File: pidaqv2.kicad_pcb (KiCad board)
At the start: 2 copper layers, 81.3 x 88.9 mm, 28 parts, among them J101 Screw_Terminal_01x11, J102 Screw_Terminal_01x06, J103 Conn_01x02_Male, J104 Screw_Terminal_01x04, J105 Screw_Terminal_01x08, U201 ADS1261BIRHBR, U301 ADS1261BIRHBR, U401 AD8426ACPZ-R7

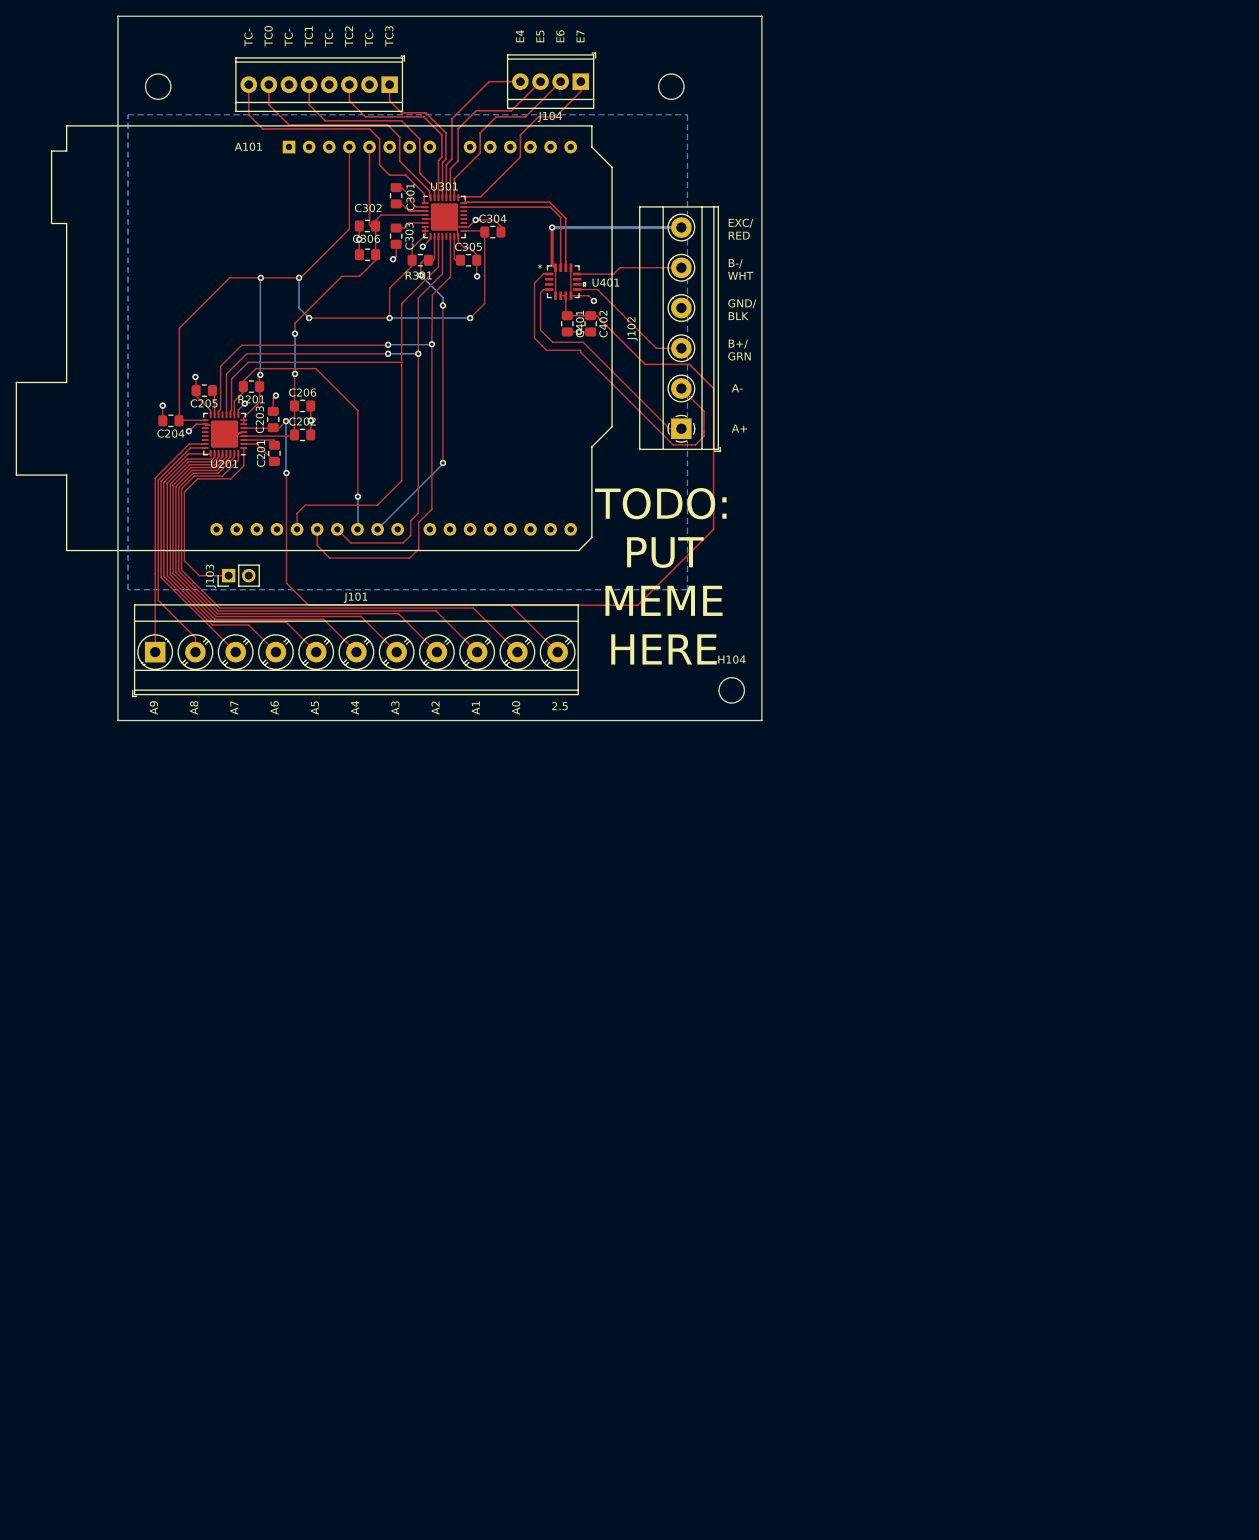
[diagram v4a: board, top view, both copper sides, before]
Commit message: placed general sensors chip
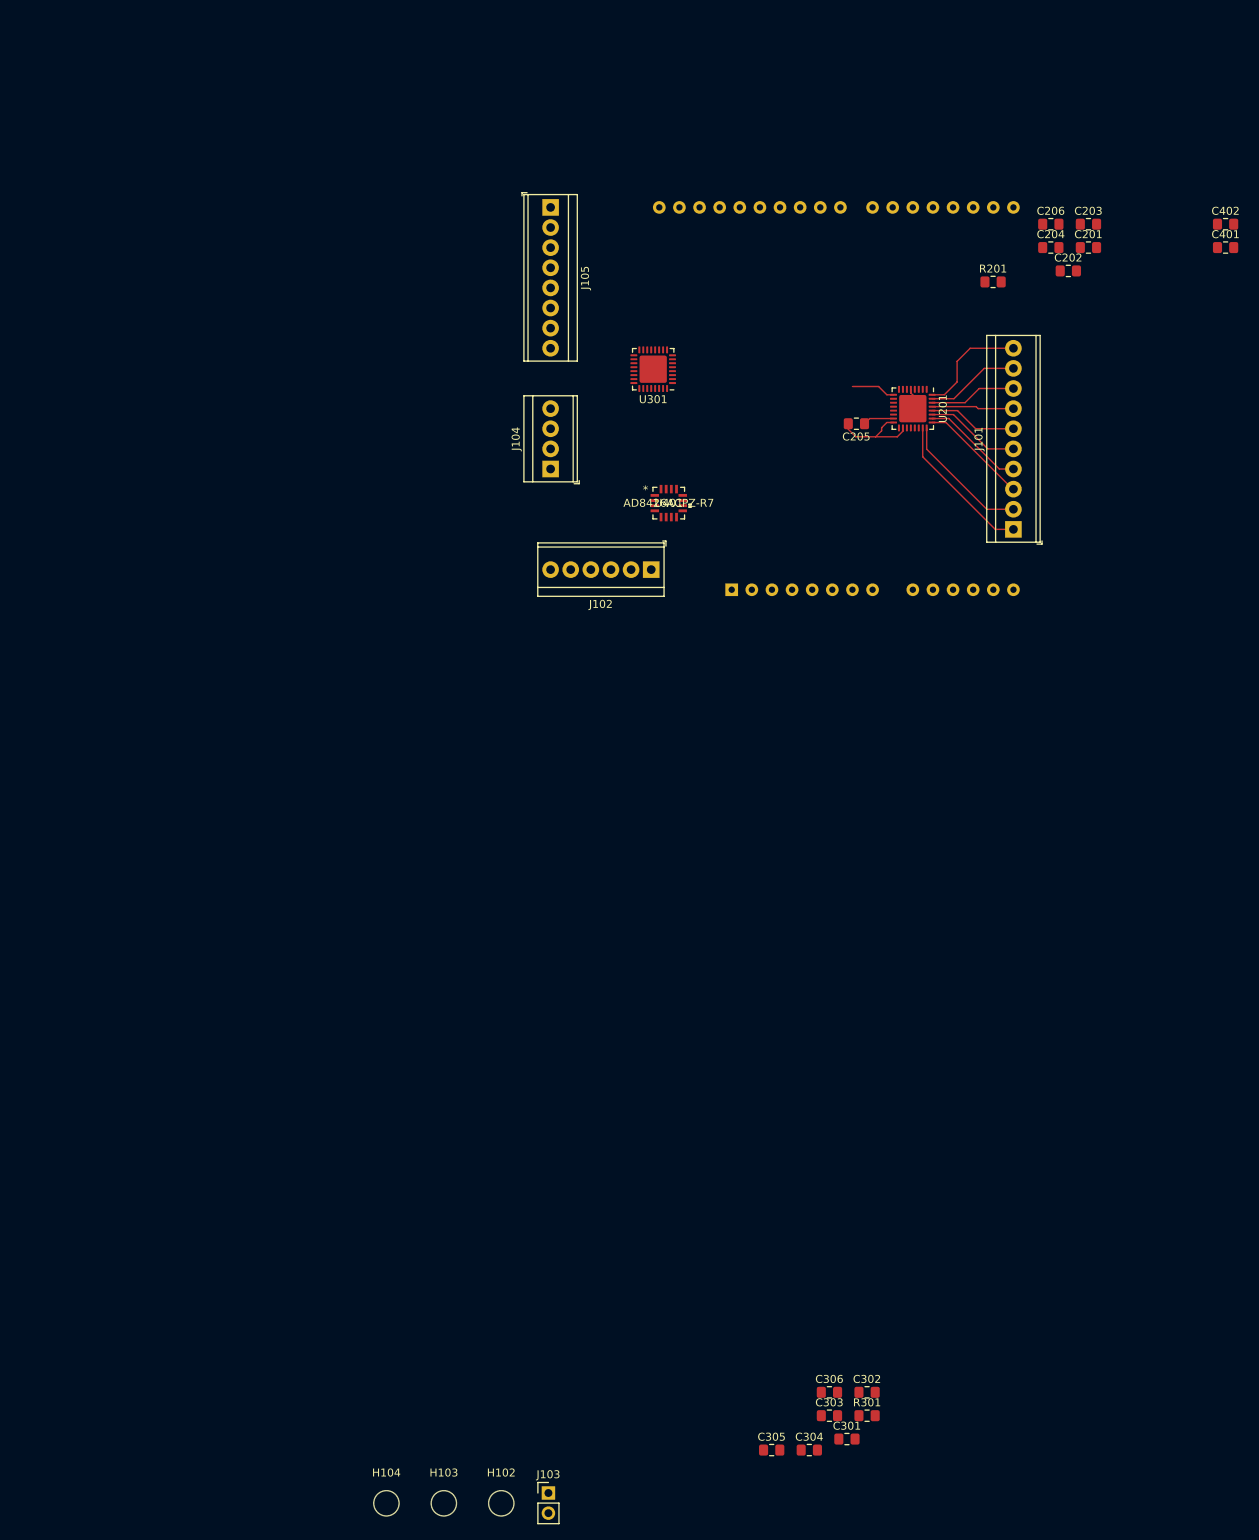
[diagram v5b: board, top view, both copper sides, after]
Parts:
- A101: moved to B.Cu
- J101: value Screw_Terminal_01x11 -> Screw_Terminal_01x10; footprint TerminalBlock_Phoenix:TerminalBlock_Phoenix_MKDS-3-11-5.08_1x11_P5.08mm_Horizontal -> TerminalBlock_TE-Connectivity:TerminalBlock_TE_1-282834-0_1x10_P2.54mm_Horizontal
- J102: footprint TerminalBlock_Phoenix:TerminalBlock_Phoenix_MKDS-1,5-6-5.08_1x06_P5.08mm_Horizontal -> TerminalBlock_TE-Connectivity:TerminalBlock_TE_282834-6_1x06_P2.54mm_Horizontal
- moved H103 182.4 mm to (105.9, 242.3)
- moved H102 180.1 mm to (113.2, 242.3)
- moved C301 166.9 mm to (156.8, 234.2), turned to 0 degrees
- moved C302 160.2 mm to (159.3, 228.3), turned to 0 degrees
- moved C304 158.8 mm to (152.0, 235.6)
- moved C303 158.6 mm to (154.6, 231.3), turned to 0 degrees
- moved R301 156.4 mm to (159.3, 231.3)
- moved C305 155.0 mm to (147.3, 235.6)
- moved C306 155.0 mm to (154.6, 228.3), turned to 0 degrees
- moved J103 122.6 mm to (119.1, 241.0), turned to 0 degrees
- moved C204 113.2 mm to (182.5, 83.8), turned to 0 degrees
- moved H104 111.5 mm to (98.7, 242.3)
- moved J101 109.4 mm to (177.8, 119.4), turned to 90 degrees
- moved C201 106.0 mm to (187.3, 83.8), turned to 0 degrees
- moved C203 105.8 mm to (187.3, 80.9), turned to 0 degrees
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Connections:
- C202 pad 2: GND -> GNDREF
- C203 pad 1: 2.5V -> /ADC0/REF2.5V
- C203 pad 2: GND -> GNDREF
- C206 pad 2: GND -> GNDREF
- C302 pad 2: GND -> GNDREF
- C303 pad 2: GND -> GNDREF
- C306 pad 2: GND -> GNDREF
- C401 pad 2: GND -> GNDREF
- C402 pad 2: GND -> GNDREF
- J102 pad 4: GND -> GNDREF
- J103 pad 2: GND -> GNDREF
- U201 pad 33: GND -> GNDREF
- U201 pad 5: GND -> GNDREF
- U201 pad 6: 2.5V -> /ADC0/REF2.5V
- U301 pad 33: GND -> GNDREF
- U301 pad 5: GND -> GNDREF
- U401 pad 13: GND -> GNDREF
- U401 pad 8: GND -> GNDREF
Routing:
- net 2.5V: track 138.1 -> 0.00 mm, vias 2 -> 0
- net +3V3: track 125.3 -> 0.00 mm, vias 6 -> 0
- net MISO: track 91.1 -> 0.00 mm, vias 2 -> 0
- net MOSI: track 80.3 -> 0.00 mm, vias 2 -> 0
- net SCLK: track 77.1 -> 0.00 mm
- net +5V: track 56.3 -> 0.00 mm, vias 2 -> 0
- net /ADC0/AIN0: track 66.5 -> 14.2 mm
- net /ADC0/AIN1: track 61.5 -> 11.8 mm
- net /ADC0/AIN2: track 56.8 -> 11.0 mm
- net /amplifier/A-: track 44.1 -> 0.00 mm
- net GND: track 61.2 -> 17.5 mm, vias 13 -> 0
- net ~CS1: track 43.0 -> 0.00 mm, vias 3 -> 0
- net /ADC0/AIN3: track 52.1 -> 10.4 mm
- net ~CS0: track 37.0 -> 0.00 mm, vias 1 -> 0
- net /ADC0/AIN4: track 47.9 -> 11.2 mm
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- removed copper zone on B.Cu, net GND
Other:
- board outline removed
- board text removed: "2.5"
- board text removed: "A+"
- board text removed: "A-"
- board text removed: "A0"
- board text removed: "A1"
- board text removed: "A2"
- board text removed: "A3"
- board text removed: "A4"
- board text removed: "A5"
- board text removed: "A6"
- board text removed: "A7"
- board text removed: "A8"
- board text removed: "A9"
- board text removed: "B+/ GRN"
- board text removed: "B-/ WHT"
- board text removed: "E4"
- board text removed: "E5"
- board text removed: "E6"
- board text removed: "E7"
- board text removed: "EXC/ RED"
- board text removed: "GND/ BLK"
- board text removed: "TC-"
- board text removed: "TC0"
- board text removed: "TC1"
- board text removed: "TC2"
- board text removed: "TC3"
- board text removed: "TODO: PUT MEME HERE"

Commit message: placed digital gnd plane
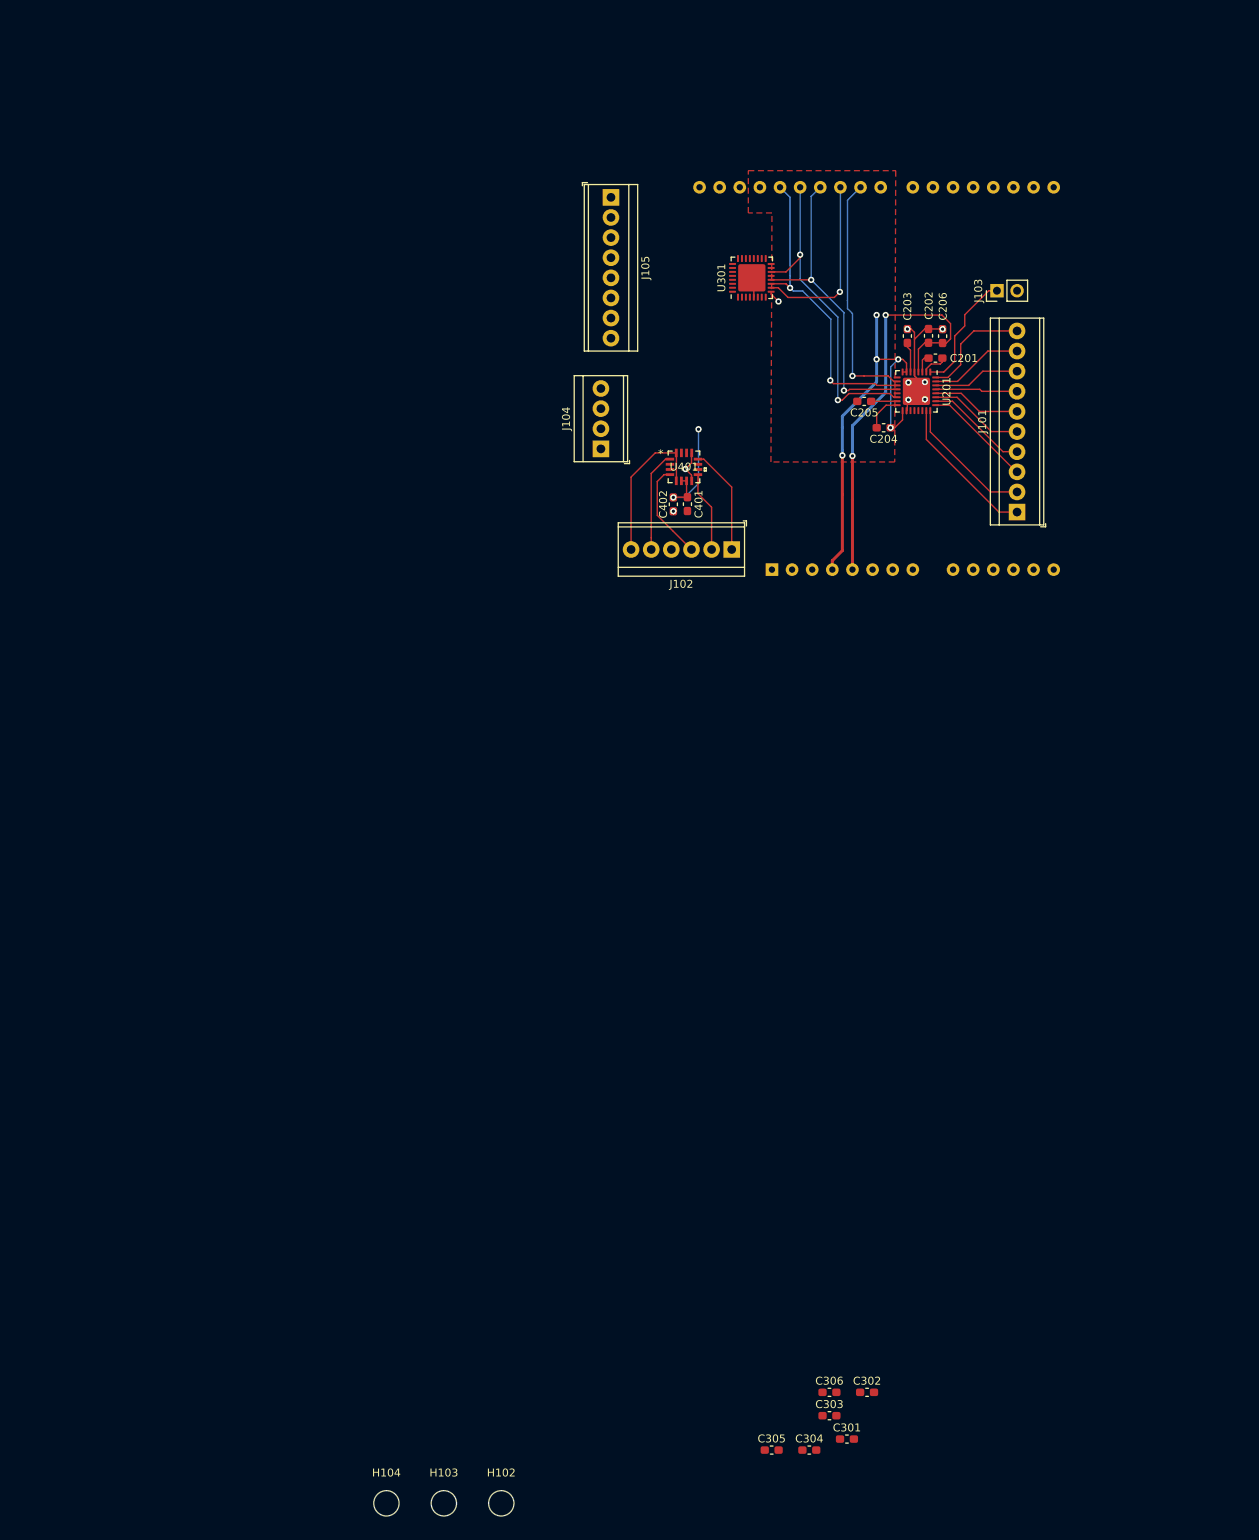
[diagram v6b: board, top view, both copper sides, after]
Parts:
- removed R201, R301: 4.7K, Resistor_SMD:R_0805_2012Metric_Pad1.15x1.40mm_HandSolder
- C201, C202, C203, C204, C205, C206, C301, C302, C303, C304, C305, C306, C401, C402: footprint Capacitor_SMD:C_0805_2012Metric_Pad1.15x1.40mm_HandSolder -> Capacitor_SMD:C_0603_1608Metric_Pad1.05x0.95mm_HandSolder
- moved J103 162.0 mm to (175.7, 89.3), turned to 90 degrees
- moved C402 78.2 mm to (134.9, 116.2), turned to 270 degrees
- moved C401 75.3 mm to (136.7, 116.2), turned to 270 degrees
- moved C204 31.0 mm to (161.4, 106.6), turned to 180 degrees
- moved C203 26.9 mm to (164.4, 95.0), turned to 90 degrees
- moved C201 23.8 mm to (168.0, 97.8), turned to 180 degrees
- moved C206 19.7 mm to (168.9, 95.0), turned to 90 degrees
- moved C202 19.5 mm to (167.1, 95.0), turned to 90 degrees
- moved U301 17.0 mm to (144.8, 87.6), turned to 90 degrees
- moved J102 10.5 mm to (142.2, 121.9)
- moved J105 7.73 mm to (127.0, 77.5)
- moved J104 6.84 mm to (125.7, 109.2)
- moved A101 5.68 mm to (147.3, 124.5)
- moved U401 4.96 mm to (136.2, 111.5)
- moved C205 2.99 mm to (159.0, 103.2)
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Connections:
- A101 pad 24: ~CS1 -> ~CS0
- A101 pad 25: ~CS0 -> ~CS1
- A101 pad 6: GND -> GNDREF
- A101 pad 7: GND -> GNDREF
- J102 pad 1: /amplifier/A+ -> /amplifier/B-
- J102 pad 2: /amplifier/A- -> /amplifier/B+
- J102 pad 3: /amplifier/B+ -> /amplifier/A+
- J102 pad 5: /amplifier/B- -> /amplifier/A-
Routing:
- net +3V3: track 0.00 -> 52.2 mm, vias 0 -> 5
- net +5V: track 0.00 -> 51.9 mm, vias 0 -> 2
- net MISO: track 0.00 -> 41.6 mm, vias 0 -> 2
- net MOSI: track 0.00 -> 39.7 mm, vias 0 -> 2
- net SCLK: track 0.00 -> 39.1 mm, vias 0 -> 2
- net ~CS0: track 0.00 -> 31.3 mm, vias 0 -> 1
- net ~CS1: track 0.00 -> 22.7 mm, vias 0 -> 1
- net /amplifier/VEXC: track 0.00 -> 19.7 mm
- net /ADC0/AINCOM: track 0.00 -> 15.3 mm
- net 2.5V: track 0.00 -> 15.3 mm, vias 0 -> 2
- net /amplifier/B-: track 0.00 -> 13.6 mm
- net /amplifier/A-: track 0.00 -> 12.7 mm
- net /amplifier/A+: track 0.00 -> 12.3 mm
- net /amplifier/B+: track 0.00 -> 10.2 mm
- net GND: track 17.5 -> 22.5 mm, vias 0 -> 7
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- added copper zone on F.Cu, net GND
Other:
- net class Power: clearance 0.2032 -> 0.1778

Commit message: temporarily complete
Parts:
- moved C304 136.6 mm to (142.7, 99.3), turned to 180 degrees
- moved C305 133.9 mm to (147.8, 101.7)
- moved C301 127.4 mm to (139.6, 108.0)
- moved C303 120.9 mm to (143.0, 110.9), turned to 270 degrees
- moved C302 119.3 mm to (138.5, 110.9), turned to 270 degrees
- moved C306 118.2 mm to (140.6, 110.9), turned to 270 degrees
- moved J105 43.3 mm to (124.5, 120.7), turned to 0 degrees
- moved J102 32.6 mm to (127.8, 92.7), turned to 90 degrees
- moved C402 30.9 mm to (133.5, 85.3), turned to 180 degrees
- moved C401 29.2 mm to (133.5, 87.1), turned to 180 degrees
- moved U401 24.9 mm to (138.2, 86.7), turned to 270 degrees
- moved U301 16.4 mm to (141.8, 103.8)
- moved J104 10.1 mm to (127.9, 99.4), turned to 270 degrees
- moved C205 1.26 mm to (160.2, 103.2)
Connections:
- A101 pad 4: +3V3 -> (no net)
- A101 pad 6: GNDREF -> GND
- A101 pad 7: GNDREF -> GND
- C202 pad 2: GNDREF -> GND
- C203 pad 2: GNDREF -> GND
- C204 pad 1: +3V3 -> +5V
- C206 pad 2: GNDREF -> GND
- C302 pad 2: GNDREF -> GND
- C303 pad 1: /ADC1/REF2.5V -> 2.5V
- C303 pad 2: GNDREF -> GND
- C304 pad 1: +3V3 -> +5V
- C306 pad 2: GNDREF -> GND
- C401 pad 2: GNDREF -> GND
- C402 pad 2: GNDREF -> GND
- J102 pad 4: GNDREF -> GND
- J103 pad 2: GNDREF -> GND
- U201 pad 17: +3V3 -> +5V
- U201 pad 33: GNDREF -> GND
- U201 pad 5: GNDREF -> GND
- U201 pad 7: +3V3 -> +5V
- U201 pad 8: +3V3 -> +5V
- U301 pad 17: +3V3 -> +5V
- U301 pad 33: GNDREF -> GND
- U301 pad 5: GNDREF -> GND
- U301 pad 6: /ADC1/REF2.5V -> 2.5V
- U301 pad 7: +3V3 -> +5V
- U301 pad 8: +3V3 -> +5V
- U401 pad 13: GNDREF -> GND
- U401 pad 8: GNDREF -> GND
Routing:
- net +5V: track 51.9 -> 114.0 mm, vias 2 -> 4
- net +3V3: track 52.2 -> 0.00 mm, vias 5 -> 0
- net /ADC1/AINCOM: track 0.00 -> 46.4 mm
- net GND: track 22.5 -> 56.0 mm, vias 7 -> 13
- net 2.5V: track 15.3 -> 43.0 mm
- net /ADC1/AIN3: track 0.00 -> 27.5 mm
- net /ADC1/AIN2: track 0.00 -> 21.7 mm
- net ~CS1: track 22.7 -> 42.2 mm, vias 1 -> 2
- net /ADC1/AIN0: track 0.00 -> 19.1 mm
- net /ADC1/AIN1: track 0.00 -> 18.8 mm
- net /A: track 0.00 -> 17.9 mm
- net /B: track 0.00 -> 16.6 mm
- net /ADC1/AIN6: track 0.00 -> 13.4 mm
- net /ADC1/AIN4: track 0.00 -> 12.9 mm
- net /ADC1/AIN7: track 0.00 -> 12.5 mm
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- added copper zone on B.Cu, net GND
- removed copper zone on F.Cu, net GND
